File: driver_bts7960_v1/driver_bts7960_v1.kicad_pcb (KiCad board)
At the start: 2 copper layers, 56.5 x 47.3 mm, 31 parts, among them J1 Motor_1, J2 Alimentacion, J6 Motor_2, J7 Conn_02x04_Odd_Even, U1 BTS7960B, U2 BTS7960B, U3 BTS7960B, U4 BTS7960B

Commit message: .
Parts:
- C5: footprint Capacitor_THT:CP_Radial_D8.0mm_P3.80mm -> Capacitor_THT:CP_Radial_D10.0mm_P5.00mm
- J1, J6: footprint Connector_AMASS:AMASS_XT30PW-M_1x02_P2.50mm_Horizontal -> Connector_AMASS:AMASS_XT30U-F_1x02_P5.0mm_Vertical
- moved J1 4.94 mm to (149.5, 58.4), turned to 180 degrees
- moved J6 4.84 mm to (161.0, 58.4), turned to 180 degrees
- moved J2 3.61 mm to (167.5, 58.4), turned to 0 degrees
- moved REF** 3.58 mm to (128.6, 56.0)
- moved REF** 3.58 mm to (178.8, 56.0)
- moved C5 3.08 mm to (136.1, 57.0)
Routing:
- net +24V: track 124.4 -> 178.6 mm
- net Net-(J6-Pin_1): track 71.3 -> 84.7 mm
- net GND: track 163.7 -> 171.3 mm
- net Net-(J1-Pin_2): track 71.5 -> 77.6 mm
- net Net-(J1-Pin_1): track 18.0 -> 23.4 mm
- net Net-(J6-Pin_2): track 18.0 -> 23.0 mm
- net ENABLE_2: track 62.0 -> 63.5 mm
- net IS_2: track 83.6 -> 84.8 mm
- net PWM_D: track 40.3 -> 41.2 mm
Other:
- board size 56.5 x 47.3 mm -> 56.5 x 43.7 mm

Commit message: .
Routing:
- net GND: track 171.3 -> 172.7 mm
- net IS_1: track 43.7 -> 44.7 mm
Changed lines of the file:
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@@
-	)
-	(segment
-		(start 127.951 69.496115)
-		(end 127.951 76.9)
-		(width 0.8)
-		(layer "B.Cu")
-		(net 1)
 	)
 	(segment
@@
 	)
 	(segment
+		(start 126.55 69.8)
+		(end 126.55 81.8)
+		(width 0.8)
+		(layer "B.Cu")
+		(net 1)
+	)
+	(segment
 		(start 173.75 76.85)
 		(end 172.35 76.85)
@@
 	)
 	(segment
+		(start 136.3 65.434246)
+		(end 136.265754 65.4)
+		(width 0.8)
+		(layer "B.Cu")
+		(net 1)
+	)
+	(segment
+		(start 136.265754 65.4)
+		(end 130.95 65.4)
+		(width 0.8)
+		(layer "B.Cu")
+		(net 1)
+	)
+	(segment
 		(start 171.8 76.3)
 		(end 171.8 71.55)
@@
 	)
 	(segment
-		(start 132.047115 65.4)
-		(end 127.951 69.496115)
-		(width 0.8)
-		(layer "B.Cu")
-		(net 1)
-	)
-	(segment
 		(start 171.8 71.55)
 		(end 172.95 70.4)
@@
 	)
 	(segment
-		(start 130.65 85.9)
-		(end 127.951 83.201)
-		(width 0.8)
-		(layer "B.Cu")
-		(net 1)
-	)
-	(segment
-		(start 136.3 65.434246)
-		(end 136.265754 65.4)
+		(start 130.95 65.4)
+		(end 126.55 69.8)
 		(width 0.8)
 		(layer "B.Cu")
@@
 	)
 	(segment
-		(start 136.265754 65.4)
-		(end 132.047115 65.4)
-		(width 0.8)
-		(layer "B.Cu")
-		(net 1)
-	)
-	(segment
-		(start 127.951 83.201)
-		(end 127.951 76.9)
+		(start 126.55 81.8)
+		(end 130.65 85.9)
 		(width 0.8)
 		(layer "B.Cu")
@@
 	(segment
 		(start 131.651 75)
-		(end 128.001 75)
-		(width 0.8)
-		(layer "B.Cu")
-		(net 1)
-	)
-	(segment
-		(start 127.951 75.05)
-		(end 127.951 76.9)
+		(end 126.55 75)
 		(width 0.8)
 		(layer "B.Cu")
@@
 		(start 172.35 76.85)
 		(end 171.8 76.3)
-		(width 0.8)
-		(layer "B.Cu")
-		(net 1)
-	)
-	(segment
-		(start 128.001 75)
-		(end 127.951 75.05)
 		(width 0.8)
 		(layer "B.Cu")
@@
 	)
 	(segment
-		(start 130.95 76.55)
-		(end 129.199 78.301)
+		(start 134.299 84.399)
+		(end 134.9 85)
+		(width 0.8)
+		(layer "B.Cu")
+		(net 7)
+	)
+	(segment
+		(start 134.627187 76.55)
+		(end 130.25 76.55)
+		(width 0.8)
+		(layer "B.Cu")
+		(net 7)
+	)
+	(segment
+		(start 148.97 89.95)
+		(end 140.45 89.95)
+		(width 0.8)
+		(layer "B.Cu")
+		(net 7)
+	)
+	(segment
+		(start 137.1 86.6)
+		(end 134.9 86.6)
+		(width 0.8)
+		(layer "B.Cu")
+		(net 7)
+	)
+	(segment
+		(start 128.475 78.325)
+		(end 128.475 82.024)
 		(width 0.8)
 		(layer "B.Cu")
@@
 	)
 	(segment
-		(start 134.627187 76.55)
-		(end 130.95 76.55)
-		(width 0.8)
-		(layer "B.Cu")
-		(net 7)
-	)
-	(segment
-		(start 134.299 84.399)
-		(end 134.9 85)
-		(width 0.8)
-		(layer "B.Cu")
-		(net 7)
-	)
-	(segment
-		(start 148.97 89.95)
-		(end 140.45 89.95)
-		(width 0.8)
-		(layer "B.Cu")
-		(net 7)
-	)
-	(segment
-		(start 129.199 78.301)
-		(end 129.199 82.748)
-		(width 0.8)
-		(layer "B.Cu")
-		(net 7)
-	)
-	(segment
-		(start 137.1 86.6)
-		(end 134.9 86.6)
-		(width 0.8)
-		(layer "B.Cu")
-		(net 7)
-	)
-	(segment
-		(start 129.199 82.748)
+		(start 140.45 89.95)
+		(end 137.1 86.6)
+		(width 0.8)
+		(layer "B.Cu")
+		(net 7)
+	)
+	(segment
+		(start 128.475 82.024)
 		(end 130.85 84.399)
+		(width 0.8)
+		(layer "B.Cu")
+		(net 7)
+	)
+	(segment
+		(start 130.25 76.55)
+		(end 128.475 78.325)
 		(width 0.8)
 		(layer "B.Cu")
@@
 		(width 0.8)
 		(layer "B.Cu")
-		(net 7)
-	)
-	(segment
-		(start 140.45 89.95)
-		(end 137.1 86.6)
-		(width 0.8)
-		(layer "B.Cu")

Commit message: .
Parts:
- removed J7: Conn_02x04_Odd_Even, Connector_PinHeader_2.54mm:PinHeader_2x04_P2.54mm_Horizontal
- added J3: Conn_02x03_Odd_Even, Connector_PinHeader_2.54mm:PinHeader_2x03_P2.54mm_Horizontal, F.Cu at (151.0, 90.0)
- added U5: 74HC244, Package_SO:SSOP-20_4.4x6.5mm_P0.65mm, F.Cu at (156.5, 92.0)
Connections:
- net IS_1 renamed Net-(U1-IS)
- net IS_2 renamed Net-(U3-IS)
- R2 pad 2: PWM_B -> OUT_B
- R3 pad 2: PWM_A -> OUT_A
- R6 pad 2: PWM_C -> OUT_C
- R8 pad 2: PWM_D -> OUT_D
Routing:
- net Net-(U3-IS): track 84.8 -> 21.2 mm
- net PWM_A: track 56.5 -> 0.00 mm, vias 1 -> 0
- net OUT_A: track 0.00 -> 53.3 mm, vias 0 -> 1
- net PWM_D: track 41.2 -> 0.00 mm, vias 1 -> 0
- net PWM_B: track 28.6 -> 0.00 mm, vias 1 -> 0
- net OUT_D: track 0.00 -> 26.1 mm, vias 0 -> 1
- net PWM_C: track 19.7 -> 0.00 mm, vias 1 -> 0
- net OUT_B: track 0.00 -> 14.3 mm, vias 0 -> 1
- net ENABLE_1: track 40.1 -> 28.0 mm
- net OUT_C: track 0.00 -> 9.35 mm, vias 0 -> 1
- net Net-(U1-IS): track 44.7 -> 36.2 mm
- net ENABLE_2: track 63.5 -> 69.8 mm
- net +24V: track 178.6 -> 184.9 mm
- net Net-(J1-Pin_2): track 77.6 -> 79.8 mm
- net Net-(J6-Pin_1): track 84.7 -> 86.7 mm

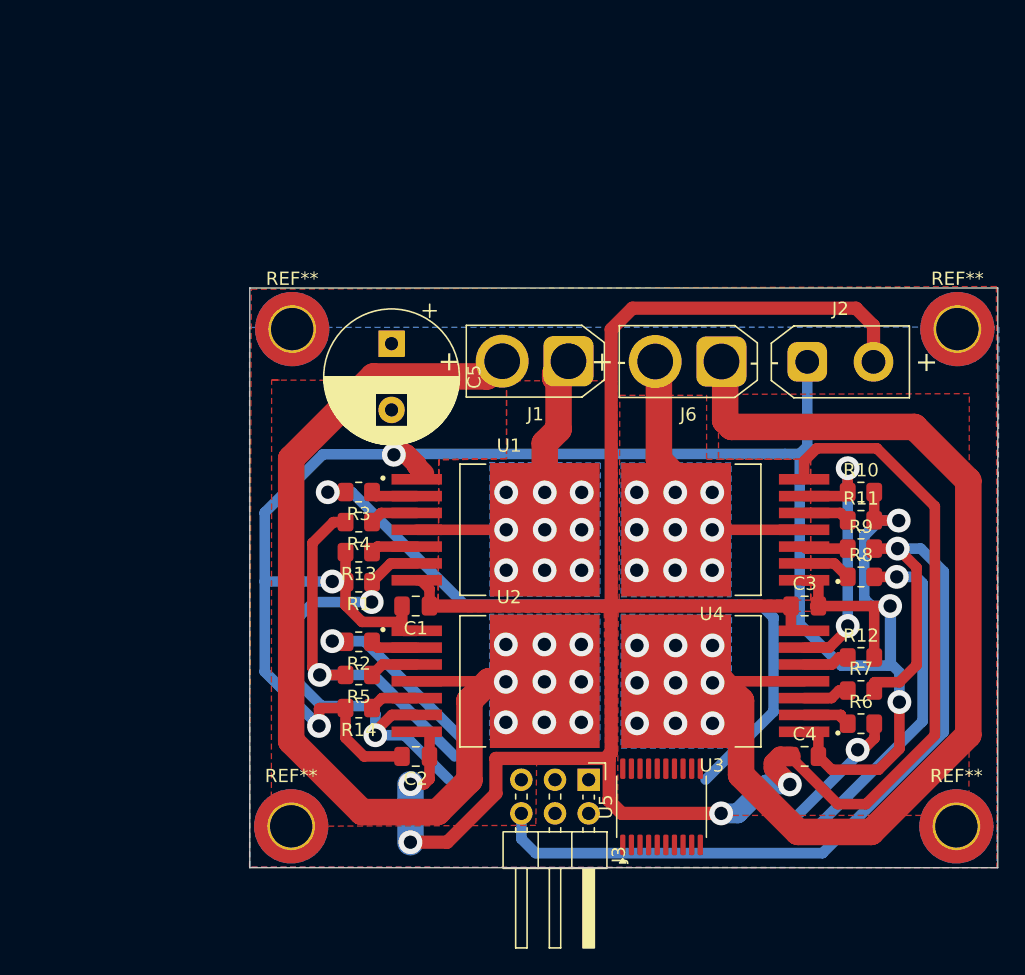
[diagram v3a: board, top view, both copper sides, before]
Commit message: v2 terminado con 74hc244
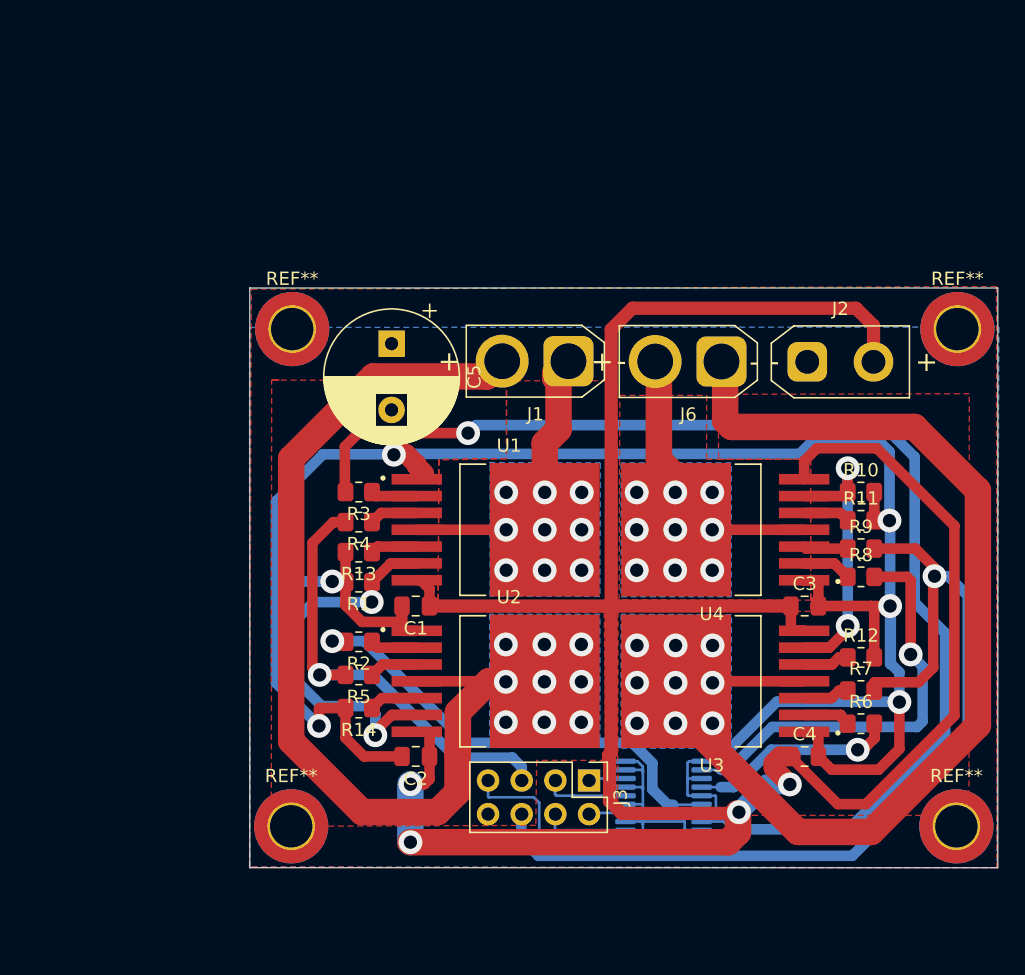
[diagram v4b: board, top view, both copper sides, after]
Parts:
- J3: value Conn_02x03_Odd_Even -> Conn_02x04_Odd_Even; footprint Connector_PinHeader_2.54mm:PinHeader_2x03_P2.54mm_Horizontal -> Connector_PinHeader_2.54mm:PinHeader_2x04_P2.54mm_Vertical
- U5: moved to B.Cu
- moved U5 0.53 mm to (156.7, 91.5), turned to 0 degrees
- moved J3 0.06 mm to (151.0, 90.0)
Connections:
- J3 pad 1: PWM_A -> PWM_D
- J3 pad 2: PWM_C -> PWM_B
- J3 pad 3: PWM_B -> PWM_C
- J3 pad 4: PWM_D -> PWM_A
- U5 pad 1: unconnected-(U5-1OE-Pad1) -> GND
- U5 pad 19: unconnected-(U5-2OE-Pad19) -> GND
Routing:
- net OUT_A: track 53.3 -> 91.5 mm
- net GND: track 172.7 -> 198.1 mm
- net OUT_B: track 14.3 -> 35.1 mm
- net +5V: track 0.00 -> 20.8 mm
- net +24V: track 184.9 -> 193.0 mm
- net Net-(U1-IS): track 36.2 -> 29.2 mm
- net PWM_A: track 0.00 -> 6.51 mm
- net ENABLE_1: track 28.0 -> 34.4 mm
- net PWM_C: track 0.00 -> 6.30 mm
- net OUT_C: track 9.35 -> 15.6 mm
- net OUT_D: track 26.1 -> 32.1 mm
- net PWM_D: track 0.00 -> 2.76 mm
- net PWM_B: track 0.00 -> 2.74 mm
- net ENABLE_2: track 69.8 -> 72.0 mm
- net Net-(J6-Pin_1): track 86.7 -> 85.3 mm

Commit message: .
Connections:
- R4 pad 2: ENABLE_1 -> OUT_EN_1
- R5 pad 2: ENABLE_1 -> OUT_EN_1
- R7 pad 2: ENABLE_2 -> OUT_EN_2
- R9 pad 2: ENABLE_2 -> OUT_EN_2
- U5 pad 15: GND -> ENABLE_2
- U5 pad 17: GND -> ENABLE_1
- U5 pad 3: GND -> OUT_EN_1
- U5 pad 5: GND -> OUT_EN_2

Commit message: .
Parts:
- removed J3: Conn_02x04_Odd_Even, Connector_PinHeader_2.54mm:PinHeader_2x04_P2.54mm_Vertical
- removed the REF** at (178.8, 93.5)
- removed the REF** at (128.6, 56.0)
- removed the REF** at (178.8, 56.0)
- removed the REF** at (128.6, 93.5)
- added J7: Conn_02x04_Odd_Even, Connector_PinHeader_2.54mm:PinHeader_2x04_P2.54mm_Vertical, F.Cu at (127.1, 72.0)
- added REF**: MountingHole_3.2mm_M3_DIN965_Pad_TopBottom, MountingHole:MountingHole_3.2mm_M3_DIN965_Pad_TopBottom, F.Cu at (158.8, 38.4)
- added REF**: MountingHole_3.2mm_M3_DIN965_Pad_TopBottom, MountingHole:MountingHole_3.2mm_M3_DIN965_Pad_TopBottom, F.Cu at (111.9, 38.4)
- added REF**: MountingHole_3.2mm_M3_DIN965_Pad_TopBottom, MountingHole:MountingHole_3.2mm_M3_DIN965_Pad_TopBottom, F.Cu at (111.9, 73.6)
- added REF**: MountingHole_3.2mm_M3_DIN965_Pad_TopBottom, MountingHole:MountingHole_3.2mm_M3_DIN965_Pad_TopBottom, F.Cu at (158.8, 73.5)
- C5: footprint Capacitor_THT:CP_Radial_D10.0mm_P5.00mm -> Capacitor_THT:CP_Radial_D8.0mm_P3.80mm
- J1, J6: moved to B.Cu
- J2: value Alimentacion -> XT30; footprint Connector_AMASS:AMASS_XT30UPB-F_1x02_P5.0mm_Vertical -> Connector_AMASS:AMASS_XT30U-F_1x02_P5.0mm_Vertical
- U5: moved to F.Cu
- moved R6 43.3 mm to (136.2, 60.8), turned to -90 degrees
- moved R7 40.1 mm to (138.4, 60.8), turned to -90 degrees
- moved U3 38.6 mm to (139.5, 50.6), turned to 90 degrees
- moved R12 36.9 mm to (140.5, 60.8), turned to -90 degrees
- moved U2 35.4 mm to (128.6, 50.6), turned to 90 degrees
- moved U1 33.4 mm to (117.6, 50.6), turned to 90 degrees
- moved C4 33.3 mm to (156.0, 56.9), turned to 90 degrees
- moved J1 32.7 mm to (123.6, 38.4), turned to 0 degrees
- moved C2 31.5 mm to (134.1, 56.9), turned to 90 degrees
- moved C3 29.9 mm to (145.0, 56.9), turned to 90 degrees
- moved R10 29.8 mm to (142.7, 60.8), turned to -90 degrees
- moved J6 29.4 mm to (139.5, 38.4), turned to 0 degrees
- moved R8 28.0 mm to (147.3, 60.8), turned to -90 degrees
- moved U5 26.1 mm to (139.6, 71.7), turned to 90 degrees
- moved R9 25.0 mm to (149.5, 60.8), turned to -90 degrees
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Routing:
- net +24V: track 193.0 -> 79.9 mm, vias 4 -> 5
- net Net-(J6-Pin_1): track 85.3 -> 8.57 mm
- net Net-(J1-Pin_2): track 79.8 -> 8.66 mm
- net OUT_A: track 91.5 -> 28.7 mm, vias 1 -> 0
- net OUT_EN_2: track 0.00 -> 43.6 mm, vias 0 -> 3
- net OUT_EN_1: track 0.00 -> 37.5 mm, vias 0 -> 3
- net ENABLE_2: track 72.0 -> 43.5 mm
- net OUT_D: track 32.1 -> 10.7 mm, vias 1 -> 0
- net PWM_D: track 2.76 -> 21.7 mm, vias 0 -> 1
- net GND: track 198.1 -> 181.6 mm, vias 6 -> 11
- net OUT_B: track 35.1 -> 18.7 mm, vias 1 -> 0
- net PWM_B: track 2.74 -> 13.8 mm, vias 0 -> 1
- net PWM_C: track 6.30 -> 16.5 mm, vias 0 -> 1
- net ENABLE_1: track 34.4 -> 24.3 mm
- net PWM_A: track 6.51 -> 16.2 mm, vias 0 -> 1
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- added copper zone on B.Cu, net +24V
- added copper zone on F.Cu, net GND
- removed copper zone on F.Cu, net +24V
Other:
- board size 56.5 x 43.7 mm -> 53.4 x 42.1 mm
- board text added: "Made by Aiden MP"

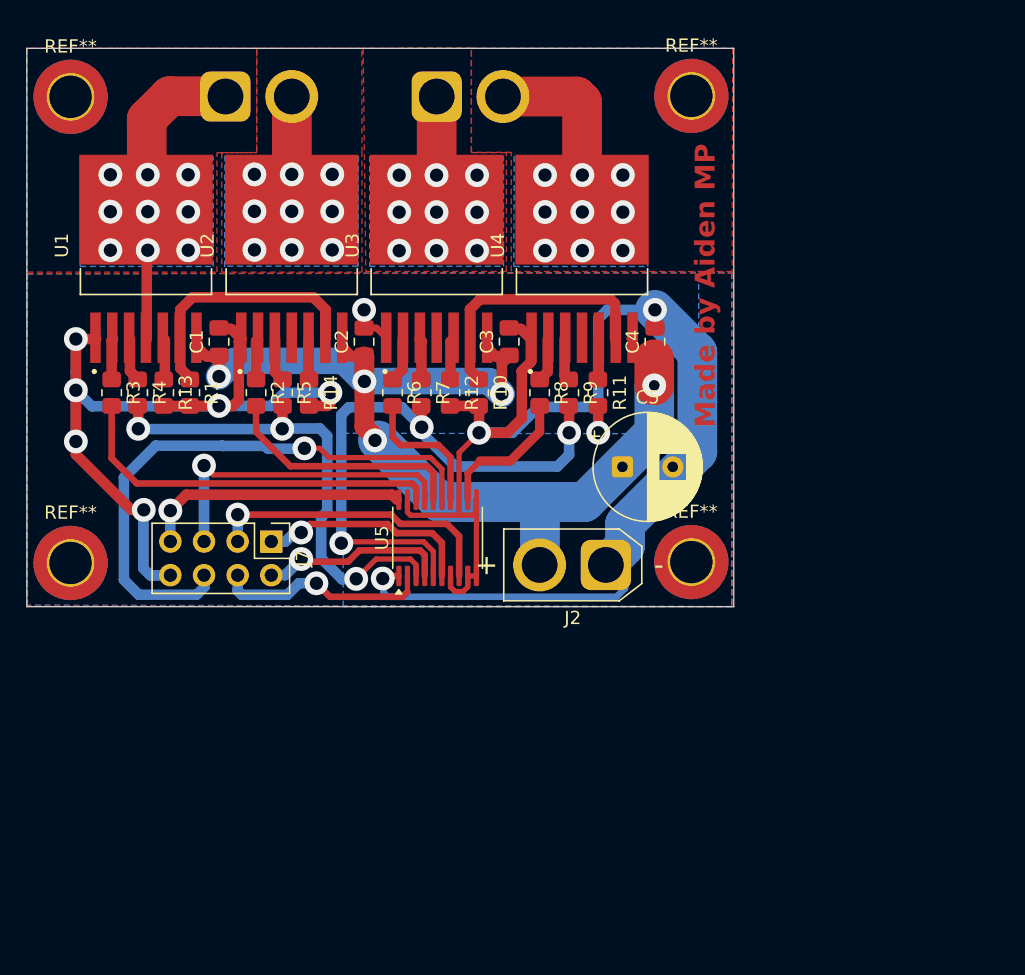
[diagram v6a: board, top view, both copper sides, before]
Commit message: footprint 74hc244 corregido
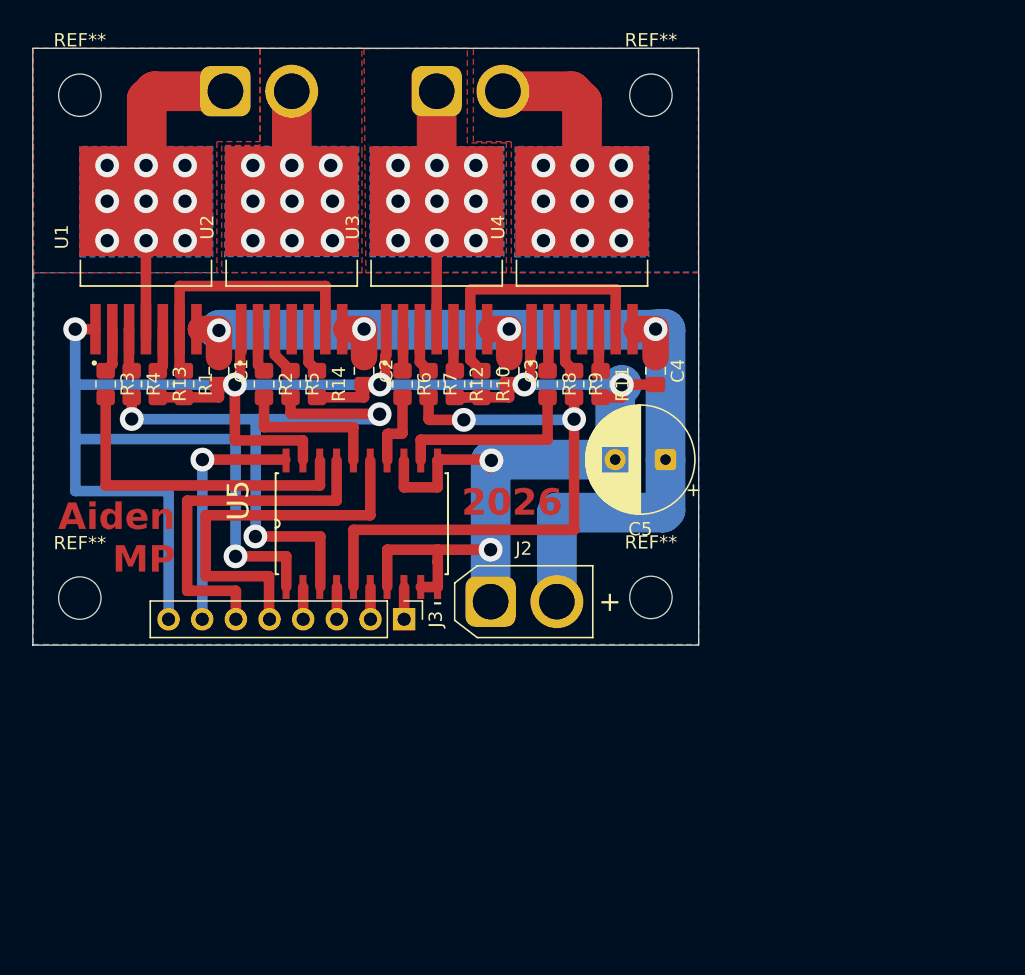
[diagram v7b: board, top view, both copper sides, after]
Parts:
- removed J7: Conn_02x04_Odd_Even, Connector_PinHeader_2.54mm:PinHeader_2x04_P2.54mm_Vertical
- removed the REF** at (158.8, 38.4)
- removed the REF** at (111.9, 38.4)
- removed the REF** at (111.9, 73.6)
- removed the REF** at (158.8, 73.5)
- added J3: Conn_01x08_Pin, Connector_PinHeader_2.54mm:PinHeader_1x08_P2.54mm_Vertical, F.Cu at (137.1, 77.8)
- added REF**: MountingHole_3.2mm_M3, MountingHole:MountingHole_3.2mm_M3, F.Cu at (112.6, 76.2)
- added REF**: MountingHole_3.2mm_M3, MountingHole:MountingHole_3.2mm_M3, F.Cu at (155.7, 38.3)
- added REF**: MountingHole_3.2mm_M3, MountingHole:MountingHole_3.2mm_M3, F.Cu at (155.7, 76.2)
- added REF**: MountingHole_3.2mm_M3, MountingHole:MountingHole_3.2mm_M3, F.Cu at (112.6, 38.3)
- U5: footprint Package_SO:SSOP-20_4.4x6.5mm_P0.65mm -> 74HC244D_653:SOIC127P1032X265-20N
- moved J2 9.13 mm to (143.6, 76.5), turned to 0 degrees
- moved U5 5.82 mm to (133.9, 70.6)
- moved C5 3.30 mm to (156.8, 65.8), turned to 180 degrees
- moved C4 2.20 mm to (156.1, 59.1), turned to -90 degrees
- moved C1 2.20 mm to (123.1, 59.1), turned to -90 degrees
- moved C2 2.20 mm to (134.1, 59.1), turned to -90 degrees
- moved C3 2.20 mm to (145.0, 59.1), turned to -90 degrees
- moved R6 0.99 mm to (136.9, 60.1)
- moved R14 0.88 mm to (130.5, 60.1)
- moved R2 0.88 mm to (126.5, 60.1)
- moved R5 0.88 mm to (128.5, 60.1)
- moved R8 0.88 mm to (147.9, 60.1)
- moved R7 0.85 mm to (138.9, 60.1)
- moved R1 0.79 mm to (120.5, 60.1)
- moved R13 0.79 mm to (118.5, 60.1)
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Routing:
- net PWM_D: track 21.7 -> 2.41 mm, vias 1 -> 0
- net GND: track 181.6 -> 200.2 mm, vias 11 -> 8
- net ENABLE_2: track 43.5 -> 29.1 mm, vias 1 -> 0
- net PWM_C: track 16.5 -> 2.41 mm, vias 1 -> 0
- net PWM_A: track 16.2 -> 2.41 mm, vias 1 -> 0
- net PWM_B: track 13.8 -> 2.35 mm, vias 1 -> 0
- net OUT_EN_1: track 37.5 -> 46.7 mm
- net OUT_B: track 18.7 -> 11.5 mm
- net Net-(J6-Pin_1): track 8.57 -> 15.0 mm
- net OUT_C: track 10.6 -> 5.84 mm
- net OUT_A: track 28.7 -> 24.7 mm
- net +24V: track 79.9 -> 76.0 mm, vias 5 -> 4
- net OUT_D: track 10.7 -> 14.3 mm
- net ENABLE_1: track 24.3 -> 26.9 mm, vias 1 -> 0
- net +5V: track 20.1 -> 18.3 mm
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- removed copper zone on B.Cu, net +24V
- removed copper zone on F.Cu, net GND
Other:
- board size 53.4 x 42.1 mm -> 50.3 x 45 mm
- board text added: "2026"
- board text added: "Aiden MP"
- board text removed: "Made by Aiden MP"
